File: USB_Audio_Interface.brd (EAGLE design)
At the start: 64.5 x 39 mm, 59 parts, among them IC1 PCM2904DB, IC2 OPA2353, IC3 AZ1117CH-ADJTRG1, J3 629722000214, Q1 12MHz

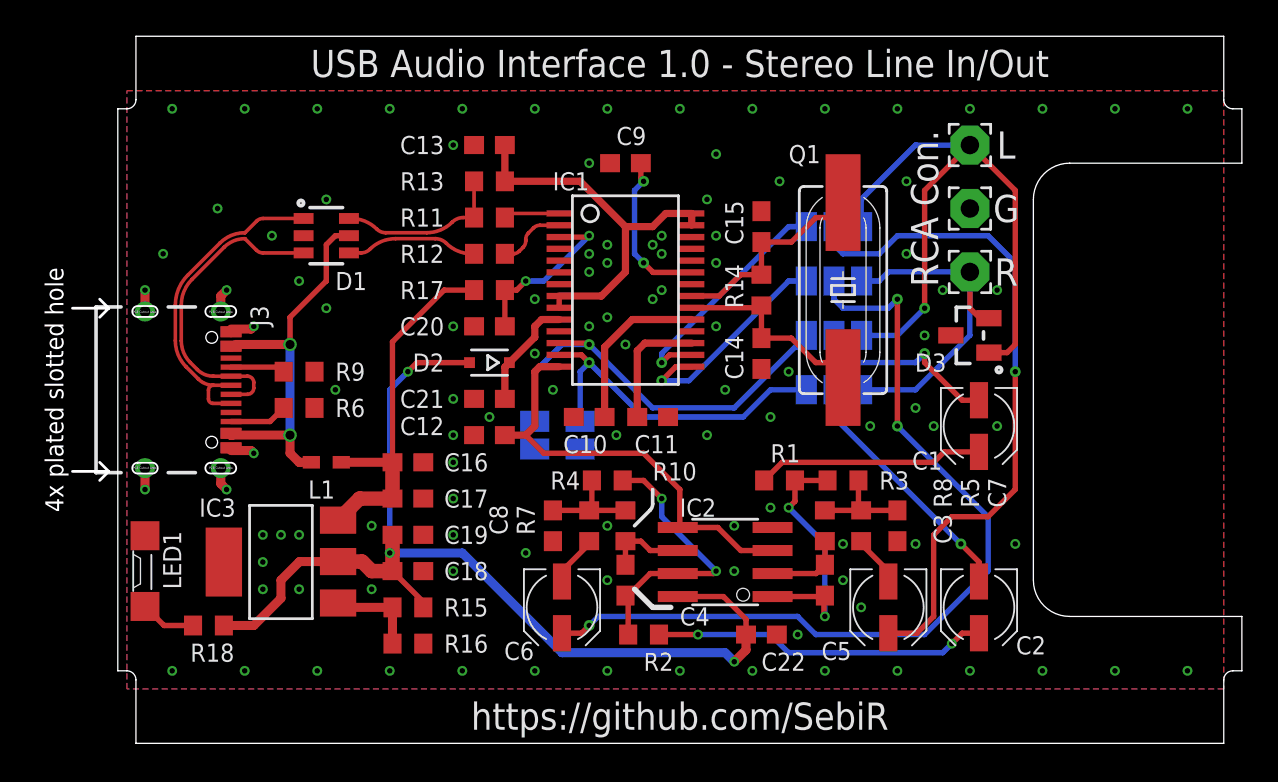
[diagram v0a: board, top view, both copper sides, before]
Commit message: * Cleaned schematic a bit, exported new PDF * Cleaned up the PCB, USB has now its own netclass, updated GERBER * Updated image of PCB * Updated readme
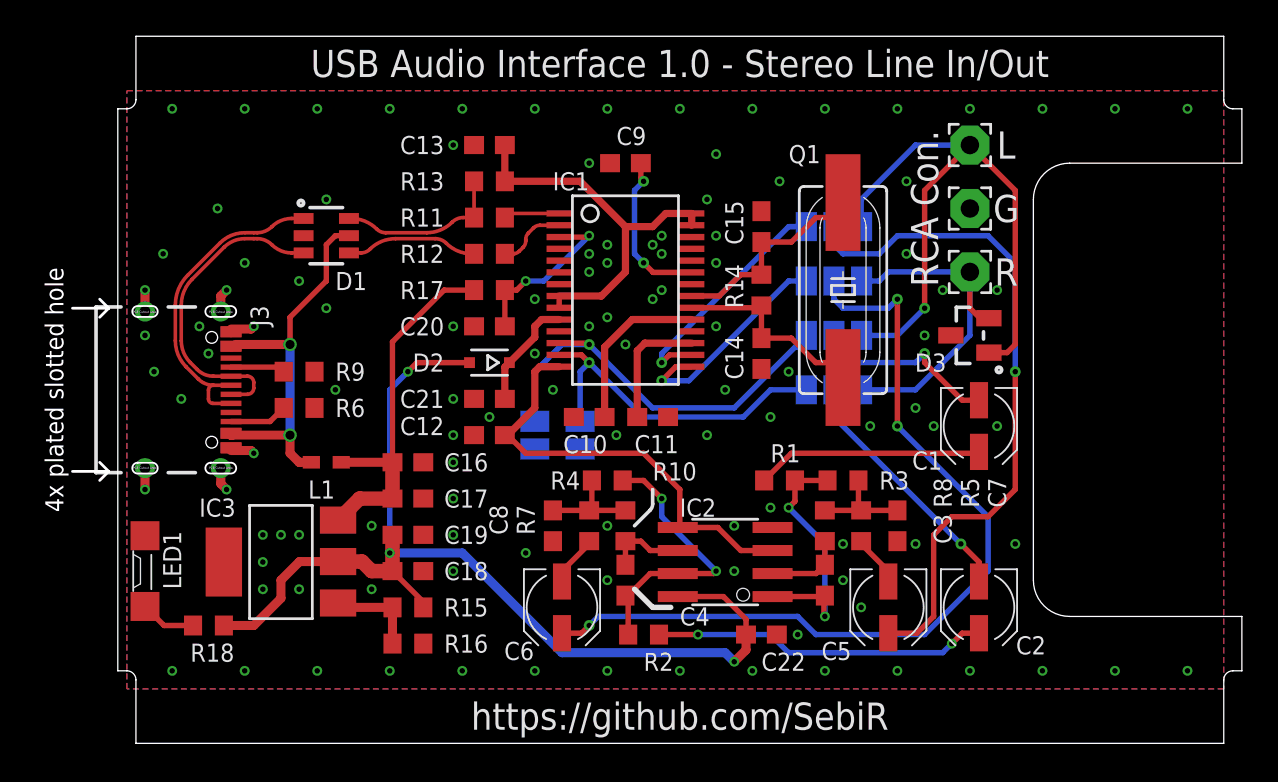
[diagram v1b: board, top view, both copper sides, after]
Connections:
- net N$18 renamed !SSPND
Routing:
- net GND: vias 108 -> 113
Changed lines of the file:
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@@
 <drawing>
 <settings>
-<setting alwaysvectorfont="yes"/>
+<setting alwaysvectorfont="no"/>
 <setting verticaltext="up"/>
 </settings>
@@
 <wire x1="30" y1="11.905" x2="29.8838" y2="11.905" width="0.3" layer="1"/>
 <wire x1="33.365" y1="10.635" x2="32.095" y2="11.905" width="0.3" layer="1"/>
-<wire x1="20.35" y1="17" x2="21.5" y2="17" width="0.4" layer="1"/>
-<wire x1="22" y1="17.5" x2="21.5" y2="17" width="0.4" layer="1"/>
+<wire x1="20.35" y1="17" x2="20.5" y2="17" width="0.4" layer="1"/>
+<wire x1="22" y1="18.5" x2="20.5" y2="17" width="0.4" layer="1"/>
 <wire x1="23.344" y1="20.775" x2="22.275" y2="20.775" width="0.4" layer="1"/>
 <wire x1="22.275" y1="20.775" x2="22" y2="20.5" width="0.4" layer="1"/>
-<wire x1="22" y1="20.5" x2="22" y2="17.5" width="0.4" layer="1"/>
+<wire x1="22" y1="20.5" x2="22" y2="18.5" width="0.4" layer="1"/>
 <wire x1="28" y1="16" x2="30" y2="14" width="0.3" layer="1"/>
 <wire x1="30" y1="14" x2="30" y2="11.905" width="0.3" layer="1"/>
-<wire x1="21.5" y1="17" x2="22.5" y2="16" width="0.3" layer="1"/>
-<wire x1="22.5" y1="16" x2="28" y2="16" width="0.3" layer="1"/>
+<wire x1="20.5" y1="17" x2="21.5" y2="16" width="0.3" layer="1"/>
+<wire x1="21.5" y1="16" x2="28" y2="16" width="0.3" layer="1"/>
 </signal>
 <signal name="+5V">
@@
 <wire x1="5.245" y1="16.45" x2="5.245" y2="16.15" width="0.3" layer="1"/>
 <contactref element="D1" pad="2"/>
-<via x="7.5" y="28" extent="1-16" drill="0.3"/>
 <via x="5" y="25" extent="1-16" drill="0.3"/>
 <via x="0.5" y="25" extent="1-16" drill="0.3"/>
@@
 <via x="13" y="8.5" extent="1-16" drill="0.3"/>
 <via x="13" y="12" extent="1-16" drill="0.3"/>
+<via x="6" y="26.5" extent="1-16" drill="0.3"/>
+<via x="2.5" y="19" extent="1-16" drill="0.3"/>
+<via x="1" y="20.5" extent="1-16" drill="0.3"/>
+<via x="0.5" y="22.5" extent="1-16" drill="0.3"/>
+<via x="4" y="21.5" extent="1-16" drill="0.3"/>
+<via x="3.5" y="23" extent="1-16" drill="0.3"/>
 </signal>
 <signal name="N$2">
@@
 <contactref element="J3" pad="A6"/>
 <contactref element="D1" pad="1"/>
-<wire x1="9.25" y1="28.95" x2="7.00710625" y2="28.95" width="0.2" layer="1"/>
-<wire x1="7.00710625" y1="28.95" x2="6.653553125" y2="28.803553125" width="0.2" layer="1" curve="45"/>
-<wire x1="6.653553125" y1="28.803553125" x2="6.023046875" y2="28.173046875" width="0.2" layer="1"/>
-<wire x1="6.023046875" y1="28.173046875" x2="6" y2="28.1635" width="0.2" layer="1" curve="-45"/>
 <wire x1="6" y1="28.1635" x2="4.63610625" y2="27.59855625" width="0.2" layer="1" curve="45"/>
 <wire x1="2.8545625" y1="25.8170125" x2="2.173" y2="24.171575" width="0.2" layer="1" curve="45"/>
@@
 <wire x1="4" y1="19" x2="4" y2="19.48" width="0.2" layer="1"/>
 <wire x1="4" y1="19.48" x2="4.27" y2="19.75" width="0.2" layer="1" curve="-90"/>
+<wire x1="6.5" y1="28.163496875" x2="6.032596875" y2="28.163496875" width="0.2" layer="1"/>
+<wire x1="9.25" y1="28.95" x2="8.586396875" y2="28.95" width="0.2" layer="1"/>
+<wire x1="8.586396875" y1="28.95" x2="7.5" y2="28.5" width="0.2" layer="1" curve="45"/>
+<wire x1="7.5" y1="28.5" x2="6.687609375" y2="28.163496875" width="0.2" layer="1" curve="-45"/>
+<wire x1="6.687609375" y1="28.163496875" x2="6.5" y2="28.163496875" width="0.2" layer="1"/>
+<wire x1="6" y1="28.1635" x2="6.032596875" y2="28.163496875" width="0" layer="19" extent="1-1"/>
 </signal>
 <signal name="USB_D_N" class="1">
@@
 <contactref element="J3" pad="A7"/>
 <contactref element="D1" pad="3"/>
-<wire x1="9.25" y1="27.05" x2="7.00710625" y2="27.05" width="0.2" layer="1"/>
-<wire x1="7.00710625" y1="27.05" x2="6.653553125" y2="27.196446875" width="0.2" layer="1" curve="-45"/>
-<wire x1="6.653553125" y1="27.196446875" x2="6.023046875" y2="27.826953125" width="0.2" layer="1"/>
-<wire x1="6.023046875" y1="27.826953125" x2="6" y2="27.8365" width="0.2" layer="1" curve="45"/>
 <wire x1="6" y1="27.8365" x2="4.867334375" y2="27.367334375" width="0.2" layer="1" curve="45"/>
 <wire x1="3.0857875" y1="25.5857875" x2="2.5" y2="24.171571875" width="0.2" layer="1" curve="45"/>
@@
 <wire x1="6.14644375" y1="19.25" x2="6.5" y2="19.60355625" width="0.2" layer="1" curve="90"/>
 <wire x1="6.5" y1="19.60355625" x2="6.5" y2="19.89644375" width="0.2" layer="1"/>
+<wire x1="6.032590625" y1="27.836496875" x2="6.5" y2="27.836496875" width="0.2" layer="1"/>
+<wire x1="9.25" y1="27.05" x2="8.586396875" y2="27.05" width="0.2" layer="1"/>
+<wire x1="8.586396875" y1="27.05" x2="7.5" y2="27.5" width="0.2" layer="1" curve="-45"/>
+<wire x1="7.5" y1="27.5" x2="6.687625" y2="27.836496875" width="0.2" layer="1" curve="45"/>
+<wire x1="6.687625" y1="27.836496875" x2="6.5" y2="27.836496875" width="0.2" layer="1"/>
+<wire x1="6" y1="27.8365" x2="6.032590625" y2="27.836496875" width="0" layer="19" extent="1-1"/>
 </signal>
 <signal name="N$1">
@@
 <contactref element="R1" pad="2"/>
 <contactref element="C1" pad="+"/>
-<wire x1="46.5" y1="16.075" x2="44.575" y2="16.075" width="0.3" layer="1"/>
-<wire x1="44.575" y1="16.075" x2="44" y2="15.5" width="0.3" layer="1"/>
-<wire x1="35.65" y1="15.5" x2="34.65" y2="14.5" width="0.3" layer="1"/>
-<wire x1="44" y1="15.5" x2="35.65" y2="15.5" width="0.3" layer="1"/>
+<wire x1="46.5" y1="16.075" x2="46.5" y2="16" width="0.3" layer="1"/>
+<wire x1="36.15" y1="16" x2="34.65" y2="14.5" width="0.3" layer="1"/>
+<wire x1="46.5" y1="16" x2="36.15" y2="16" width="0.3" layer="1"/>
 </signal>
 <signal name="CONN_L">
@@
 <wire x1="23.5" y1="9.5" x2="23.5" y2="8.925" width="0.3" layer="1"/>
 </signal>
-<signal name="N$18">
+<signal name="!SSPND">
 <contactref element="IC1" pad="28"/>
 <contactref element="IC1" pad="27"/>
